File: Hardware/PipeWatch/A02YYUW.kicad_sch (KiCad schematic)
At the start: 1 part, among them J2 Conn_01x04_Pin

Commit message: tweeked the Layout
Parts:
- J2: value Conn_01x04_Pin -> A02YYUW
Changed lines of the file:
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@@
 (kicad_sch
-	(version 20231120)
+	(version 20250114)
 	(generator "eeschema")
-	(generator_version "8.0")
+	(generator_version "9.0")
 	(paper "A4")
 	(wire
@@
 		(shape input)
 		(at 120.65 111.76 0)
-		(fields_autoplaced yes)
 		(effects
 			(font
@@
 		(shape input)
 		(at 120.65 109.22 0)
-		(fields_autoplaced yes)
 		(effects
 			(font
@@
 			)
 		)
-		(property "Value" "Conn_01x04_Pin"
+		(property "Value" "A02YYUW"
 			(at 116.205 101.6 0)
 			(effects

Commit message: some changes
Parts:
- J2: footprint Connector_JST:JST_PH_B4B-PH-K_1x04_P2.00mm_Vertical -> Connector_JST:JST_XH_B4B-XH-A_1x04_P2.50mm_Vertical
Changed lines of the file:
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@@
 			)
 		)
-		(property "Footprint" "Connector_JST:JST_PH_B4B-PH-K_1x04_P2.00mm_Vertical"
+		(property "Footprint" "Connector_JST:JST_XH_B4B-XH-A_1x04_P2.50mm_Vertical"
 			(at 115.57 106.68 0)
 			(effects

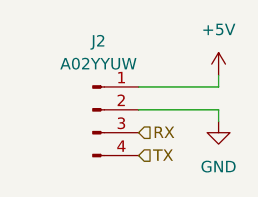
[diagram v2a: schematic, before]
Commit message: Added Ten Sensor
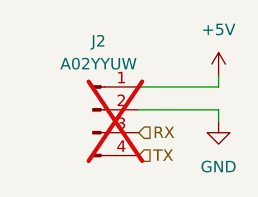
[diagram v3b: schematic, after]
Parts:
- J2: now not fitted
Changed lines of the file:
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@@
 		(in_bom yes)
 		(on_board yes)
-		(dnp no)
+		(dnp yes)
 		(fields_autoplaced yes)
 		(property "Reference" "J2"

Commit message: Changed the scematic page Labeling
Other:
- company: (none) -> Felix Pelster
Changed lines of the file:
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@@
 	(generator_version "9.0")
 	(paper "A4")
+	(title_block
+		(date "2025-09-24")
+		(company "Felix Pelster")
+	)
 	(wire
 		(pts
